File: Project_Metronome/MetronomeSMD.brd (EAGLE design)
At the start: 62.4 x 31.5 mm, 45 parts

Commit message: better eagle files
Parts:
- removed JP17, JP18: (no value), adafruit:1X09-BIG
- removed JP2: (no value), adafruit:1X03-CLEANBIG
- removed LED1: RED, adafruit:LED5MM
- removed LED2: GREEN, adafruit:LED5MM
- removed LED3: O, adafruit:CHIPLED_1206
- removed R1, R10, R11, R12, R13, R14, R15, R16, R2, R3, R4, R8, R9: 1k, resistor:R1206
- removed R5, R6, R7: 10k, resistor:R1206
- added ., ..: (no value), adafruit:1X03-CLEANBIG
- added ..., .....: (no value), adafruit:1X09-BIG
- added 1, 10, 11, 12, 13, 15, 16, 17, 18, 2, 3, 4, 9: 1k, resistor:R1206
- added 6, 7, 8: 10k, resistor:R1206
- added GREEN: GREEN, adafruit:LED5MM
- added LED: O, adafruit:CHIPLED_1206
- added RED: RED, adafruit:LED5MM
- JP1: device adafruit:1X03-CLEANBIG -> adafruit:1X06-BIGLOCK
- moved JP1 14.6 mm to (1.78, 16.5), turned to 90 degrees
- moved JP16 1.85 mm to (59.9, 18.5)
- moved C4 1.85 mm to (51.8, 27.7)
- moved JP9 1.85 mm to (59.9, 22.4)
- moved R17 1.85 mm to (43.7, 27.7)
- moved C6 1.85 mm to (28.7, 16.3)
- moved C7 1.85 mm to (28.7, 4.83)
- moved C8 1.85 mm to (28.7, 10.7)
- moved 7805 1.85 mm to (56.4, 27.9)
- moved C2 1.85 mm to (61.0, 27.9)
- moved PIC16F648A 1.85 mm to (14.7, 16.5)
- moved R21 1.85 mm to (32.0, 16.3)
- moved C1 1.85 mm to (38.4, 21.6)
- moved C3 1.85 mm to (28.4, 27.7)
- moved C5 1.85 mm to (40.6, 27.7)
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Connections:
- net GND: now also ...1, ...2, ...3, GREEN.K, JP1.3, LED.C, RED.K; no longer JP2.1, JP2.2, JP2.3, LED1.K, LED2.K, LED3.C
- net N$1: now also 9.2; no longer R8.2
- net N$10: now also ......9, 1.1; no longer JP18.9, R1.1
- net N$11: now also ......8, 2.1; no longer JP18.8, R2.1
- net N$12: now also ......7, 3.1; no longer JP18.7, R3.1
- net N$13: now also ......6, 4.1; no longer JP18.6, R4.1
- net N$14: now also ......4, 6.1; no longer JP18.4, R5.1
- net N$15: now also ......3, 7.1; no longer JP18.3, R6.1
- net N$16: now also ......2, 8.1; no longer JP18.2, R7.1
- net N$17: now also ......1, 9.1, GREEN.A; no longer JP18.1, LED2.A, R8.1
- net N$18: now also 18.1; no longer R9.1
- net N$19: now also 17.1; no longer R10.1
- net N$2: now also 1.2; no longer R1.2
- net N$20: now also 16.1; no longer R11.1
- net N$21: now also 15.1; no longer R12.1
- net N$22: now also 13.1, JP1.4; no longer R13.1
- net N$24: now also 12.1, JP1.5; no longer R14.1
- net N$26: now also 11.1; no longer R15.1
- net N$27: now also 10.1, JP1.6; no longer R16.1
- net N$28: now also ....1, 18.2; no longer JP17.1, R9.2
- net N$29: now also ....2, 17.2; no longer JP17.2, R10.2
- net N$3: now also 2.2; no longer R2.2
- net N$30: now also ....3, 16.2; no longer JP17.3, R11.2
- net N$31: now also ....4, 15.2; no longer JP17.4, R12.2
- net N$32: now also ....6, 13.2; no longer JP17.6, R13.2
- net N$34: now also ....7, 12.2; no longer JP17.7, R14.2
- net N$37: now also ....8, 11.2; no longer JP17.8, R15.2
- net N$38: now also ....9, 10.2, RED.A; no longer JP17.9, LED1.A, R16.2
- net N$4: now also 3.2; no longer R3.2
- net N$40: now also LED.A; no longer LED3.A
- net N$5: now also 4.2, JP1.1; no longer R4.2
- net N$6: now also 6.2; no longer R5.2
- net N$7: now also 7.2; no longer R6.2
- net N$8: now also 8.2; no longer R7.2
- net VDD: now also ..1, ..2, ..3; no longer JP1.1, JP1.3
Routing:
- net VDD: track 76.1 -> 102.9 mm
- net N$27: track 2.66 -> 28.0 mm
- net N$24: track 2.66 -> 24.1 mm
- net GND: track 134.6 -> 152.4 mm, vias 3 -> 5
- net N$22: track 2.66 -> 19.5 mm, vias 0 -> 1
- net N$5: track 3.05 -> 14.3 mm
- net VCC: track 36.9 -> 41.2 mm
- net N$39: track 29.8 -> 26.0 mm
- net N$7: track 17.7 -> 14.1 mm, vias 1 -> 2
- net N$17: track 43.5 -> 40.3 mm, vias 2 -> 1
- net N$38: track 30.5 -> 33.0 mm, vias 1 -> 2
- net N$25: track 4.81 -> 6.49 mm
- net N$12: track 3.18 -> 4.46 mm
- net N$10: track 3.18 -> 4.46 mm
- net N$11: track 3.18 -> 4.46 mm
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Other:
- board size 62.4 x 31.5 mm -> 63.4 x 33 mm
- board text added: "METROKNOME_2016"
- board text added: "MetroKnome"
- board text removed: "METRONOME"
- board text removed: "METRONOME_2016"

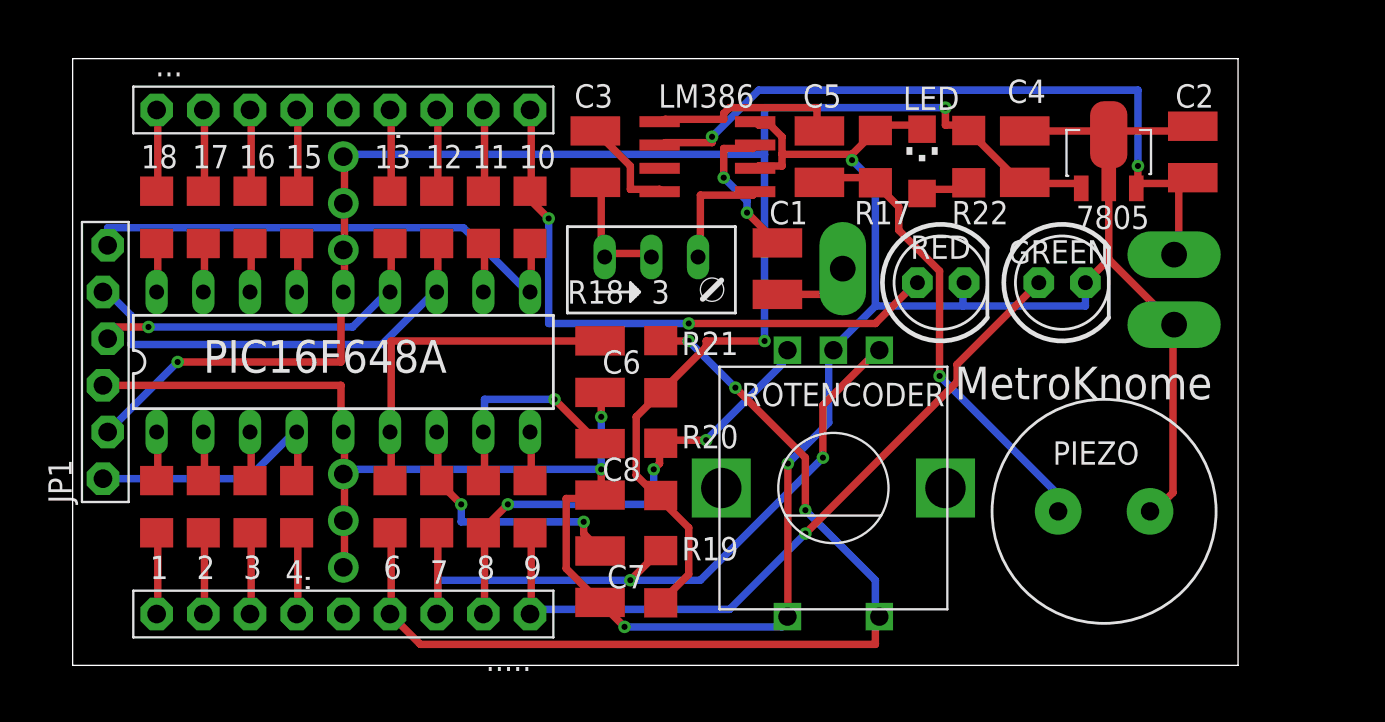
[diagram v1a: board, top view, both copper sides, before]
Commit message: better eagle files
the traces are auto trash and there is a lot of "extra parts", but the form is coming together.  Width is close to the size of enclosures I am investigating.  The short dimension can still be shrunk further.  Currently this plan is about $18 at OshPark for three boards. That's OK.
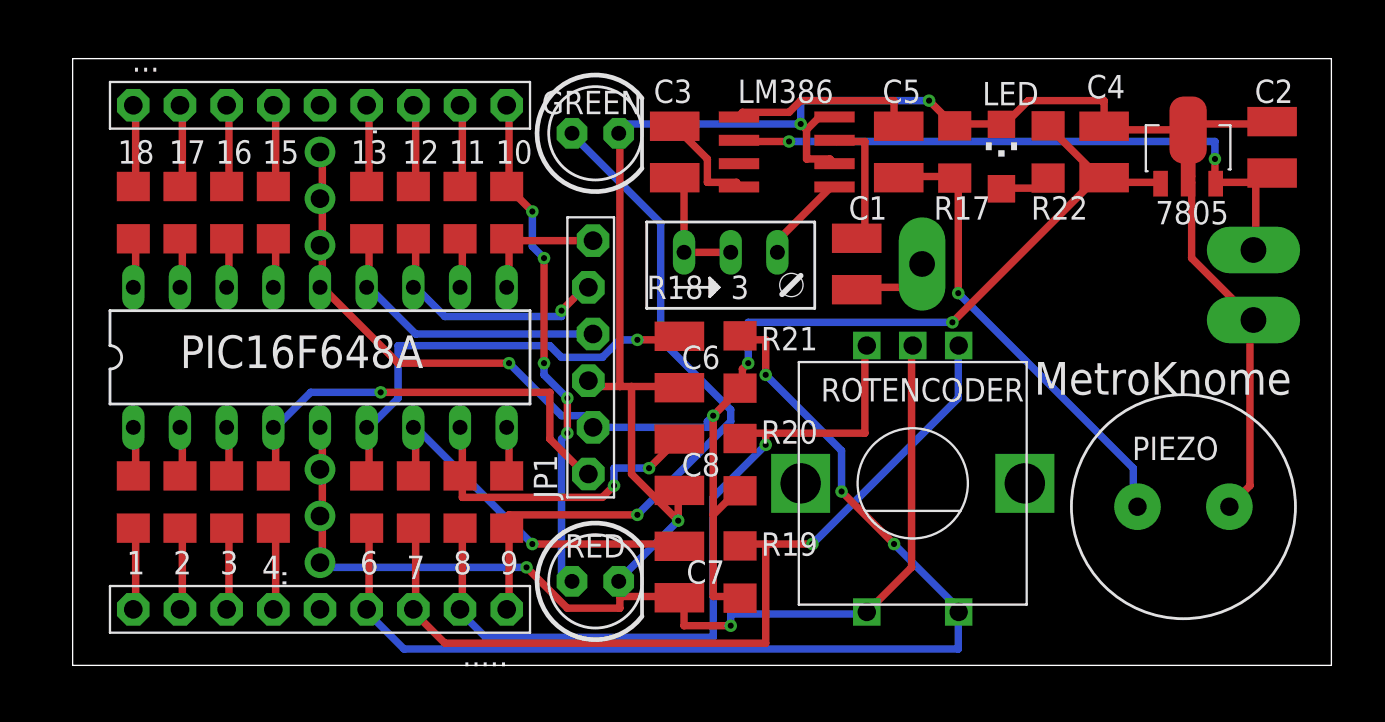
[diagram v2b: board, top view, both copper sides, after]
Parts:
- moved GREEN 26.7 mm to (28.4, 29.0)
- moved JP1 26.4 mm to (28.2, 16.8)
- moved RED 24.9 mm to (28.4, 4.57)
- moved JP7 4.33 mm to (46.2, 21.8)
- moved LM386 4.33 mm to (38.9, 27.9)
- moved R19 4.33 mm to (36.3, 5.08)
- moved R20 4.33 mm to (36.3, 10.9)
- moved R21 4.33 mm to (36.3, 16.5)
- moved 7805 4.33 mm to (60.7, 28.2)
- moved C2 4.33 mm to (65.3, 28.2)
- moved C6 4.33 mm to (33.0, 16.5)
- moved C7 4.33 mm to (33.0, 5.08)
- moved C8 4.33 mm to (33.0, 10.9)
- moved R18 4.33 mm to (35.8, 21.8)
- moved C1 4.33 mm to (42.7, 21.8)
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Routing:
- net N$27: track 28.0 -> 7.56 mm
- net VDD: track 102.9 -> 83.6 mm, vias 3 -> 4
- net N$16: track 27.3 -> 43.1 mm, vias 3 -> 1
- net N$24: track 24.1 -> 13.9 mm, vias 0 -> 1
- net N$5: track 14.3 -> 24.1 mm, vias 0 -> 1
- net GND: track 152.4 -> 161.6 mm
- net N$15: track 39.5 -> 48.0 mm, vias 2 -> 1
- net N$14: track 54.0 -> 60.4 mm
- net N$8: track 11.7 -> 17.7 mm, vias 1 -> 2
- net N$7: track 14.1 -> 20.0 mm, vias 2 -> 1
- net N$38: track 33.0 -> 27.8 mm, vias 2 -> 5
- net N$6: track 19.0 -> 24.2 mm, vias 0 -> 1
- net VCC: track 41.2 -> 36.4 mm
- net N$22: track 19.5 -> 16.2 mm, vias 1 -> 0
- net N$25: track 6.49 -> 4.93 mm
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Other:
- board size 63.4 x 33 mm -> 68.5 x 33 mm

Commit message: better eagle files
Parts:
- moved JP9 7.12 mm to (57.1, 22.4)
- moved JP16 3.59 mm to (63.8, 22.4)
- moved PIEZO 3.31 mm to (60.2, 11.9)
- moved JP7 1.61 mm to (47.8, 22.4), turned to 180 degrees
- moved ROTENCODER 0.25 mm to (45.7, 9.65)
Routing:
- net N$17: track 38.7 -> 50.2 mm, vias 1 -> 2
- net N$16: track 43.1 -> 33.5 mm, vias 1 -> 3
- net N$6: track 24.2 -> 32.8 mm
- net N$38: track 27.8 -> 33.2 mm, vias 5 -> 2
- net VCC: track 36.4 -> 40.2 mm
- net GND: track 161.6 -> 158.0 mm, vias 5 -> 3
- net N$39: track 25.5 -> 22.5 mm
- net N$85: track 4.88 -> 6.80 mm
- net N$15: track 48.0 -> 49.3 mm
- net N$5: track 24.1 -> 22.9 mm
- net N$14: track 60.4 -> 59.8 mm, vias 3 -> 2
- net N$36: track 10.4 -> 10.9 mm
- net VDD: track 83.6 -> 83.2 mm, vias 4 -> 5
- net N$7: track 20.0 -> 20.3 mm, vias 1 -> 2
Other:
- board text added: "ACORN_ENERGY_LLC"
- board text added: "METROKNOME"
- board text removed: "MetroKnome"
